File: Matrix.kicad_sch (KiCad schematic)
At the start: 28 parts

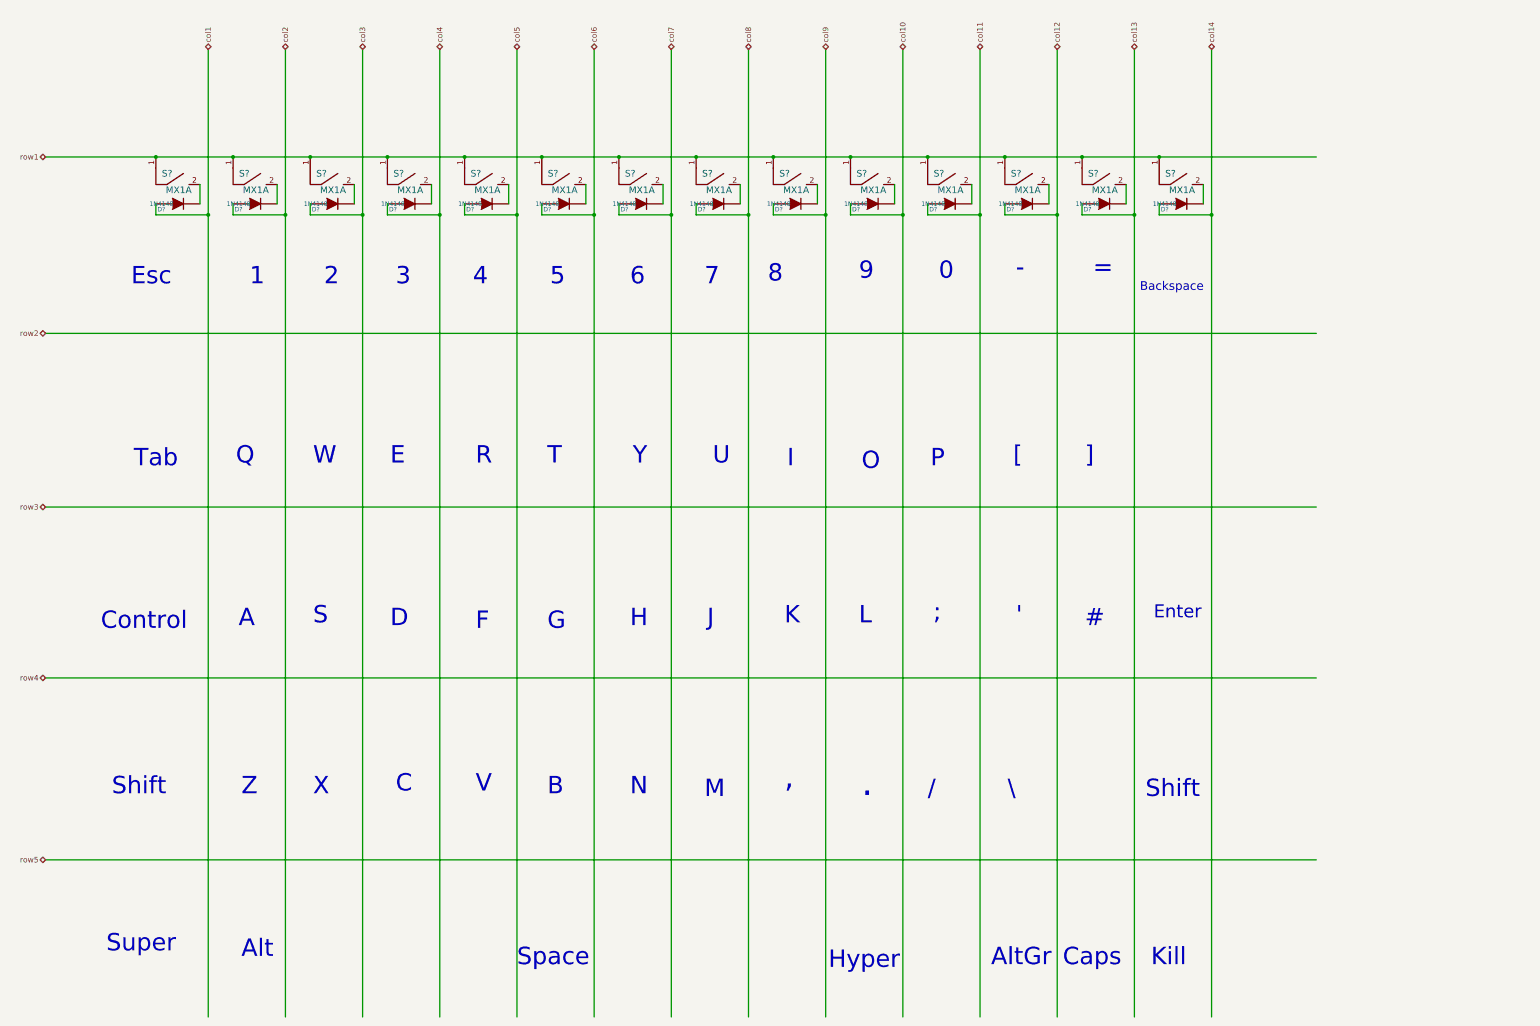
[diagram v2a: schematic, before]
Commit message: Added all remaining switches and annotations to the matrix
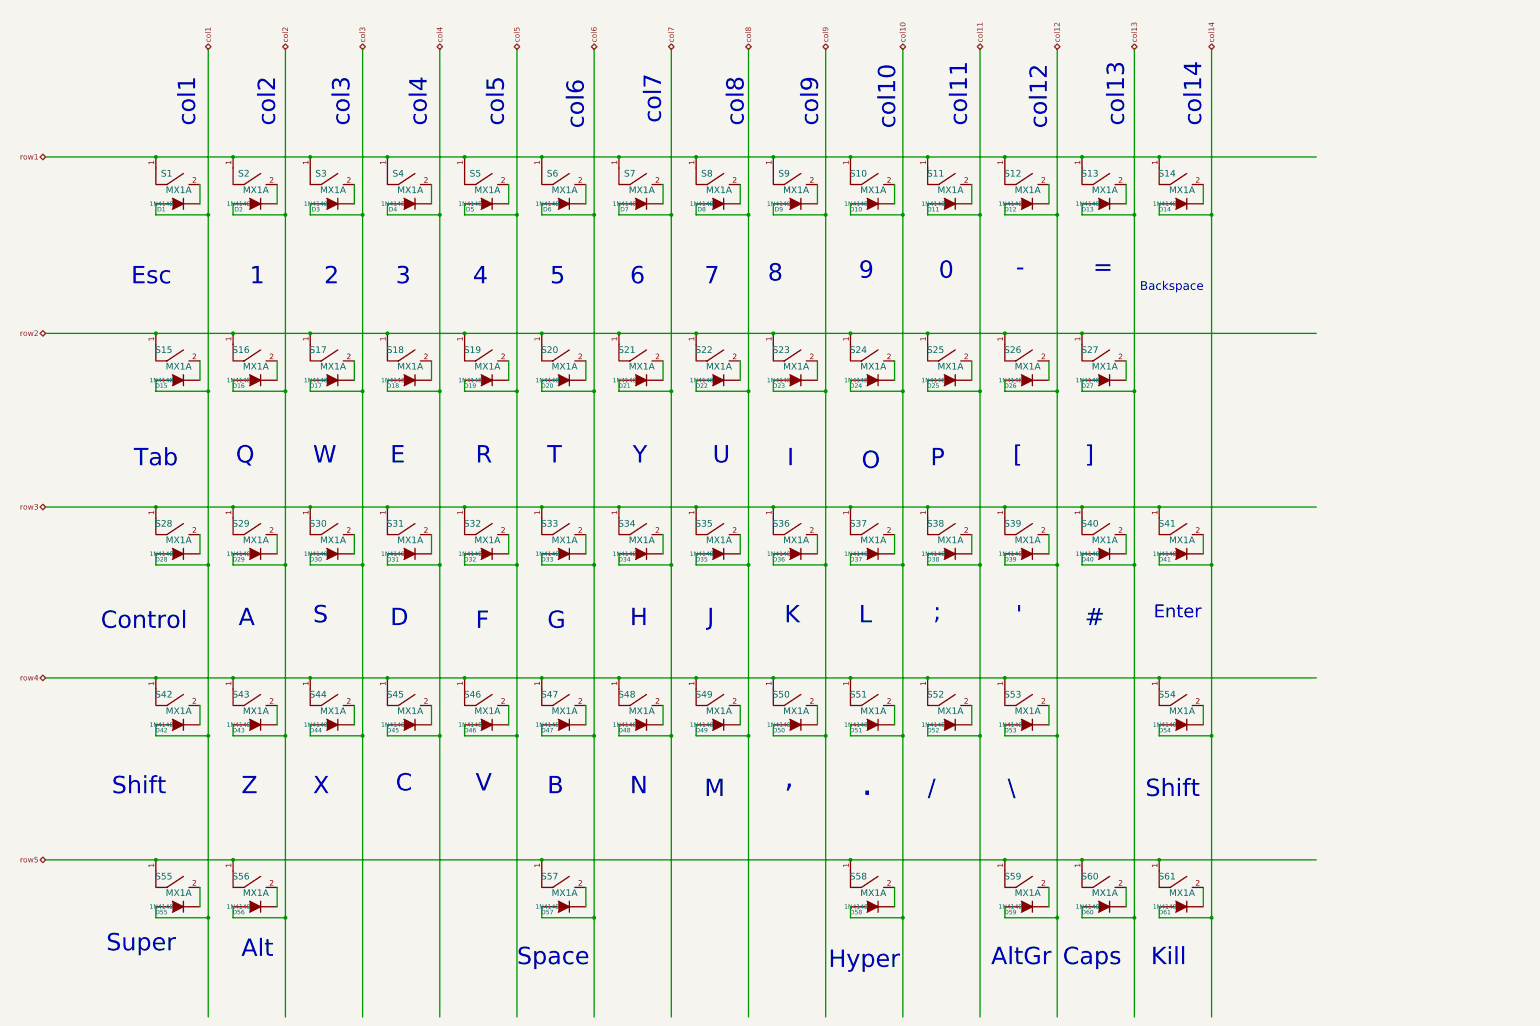
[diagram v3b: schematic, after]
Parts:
- added D15, D16, D17, D18, D19, D20, D21, D22, D23, D24, D25, D26, D27, D28, D29, D30, D31, D32, D33, D34, D35, D36, D37, D38, D39, D40, D41, D42, D43, D44, D45, D46, D47, D48, D49, D50, D51, D52, D53, D54, D55, D56, D57, D58, D59, D60, D61: 1N4148, symbol device:DIODE
- added S15, S16, S17, S18, S19, S20, S21, S22, S23, S24, S25, S26, S27, S28, S29, S30, S31, S32, S33, S34, S35, S36, S37, S38, S39, S40, S41, S42, S43, S44, S45, S46, S47, S48, S49, S50, S51, S52, S53, S54, S55, S56, S57, S58, S59, S60, S61: MX1A, symbol mx1a-simple:MX1A
- gave numbers to parts that had none: 28
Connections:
- net col1: now also D15.1 (A), D28.1 (A), D42.1 (A), D55.1 (A)
- net col10: now also D24.1 (A), D37.1 (A), D51.1 (A), D58.1 (A)
- net col11: now also D25.1 (A), D38.1 (A), D52.1 (A)
- net col12: now also D26.1 (A), D39.1 (A), D53.1 (A), D59.1 (A)
- net col13: now also D27.1 (A), D40.1 (A), D60.1 (A)
- net col14: now also D41.1 (A), D54.1 (A), D61.1 (A)
- net col2: now also D16.1 (A), D29.1 (A), D43.1 (A), D56.1 (A)
- net col3: now also D17.1 (A), D30.1 (A), D44.1 (A)
- net col4: now also D18.1 (A), D31.1 (A), D45.1 (A)
- net col5: now also D19.1 (A), D32.1 (A), D46.1 (A)
- net col6: now also D20.1 (A), D33.1 (A), D47.1 (A), D57.1 (A)
- net col7: now also D21.1 (A), D34.1 (A), D48.1 (A)
- net col8: now also D22.1 (A), D35.1 (A), D49.1 (A)
- net col9: now also D23.1 (A), D36.1 (A), D50.1 (A)
- net row2: now also S15.1, S16.1, S17.1, S18.1, S19.1, S20.1, S21.1, S22.1, S23.1, S24.1, S25.1, S26.1, S27.1
- net row3: now also S28.1, S29.1, S30.1, S31.1, S32.1, S33.1, S34.1, S35.1, S36.1, S37.1, S38.1, S39.1, S40.1, S41.1
- net row4: now also S42.1, S43.1, S44.1, S45.1, S46.1, S47.1, S48.1, S49.1, S50.1, S51.1, S52.1, S53.1, S54.1
- net row5: now also S55.1, S56.1, S57.1, S58.1, S59.1, S60.1, S61.1
- new net: D55.2 (K), S55.2
- new net: D48.2 (K), S48.2
- new net: D44.2 (K), S44.2
- new net: D32.2 (K), S32.2
- new net: D25.2 (K), S25.2
- new net: D29.2 (K), S29.2
- new net: D23.2 (K), S23.2
- new net: D21.2 (K), S21.2
- new net: D46.2 (K), S46.2
- new net: D37.2 (K), S37.2
- new net: D38.2 (K), S38.2
- new net: D19.2 (K), S19.2
- new net: D26.2 (K), S26.2
- new net: D43.2 (K), S43.2
- new net: D52.2 (K), S52.2
- new net: D31.2 (K), S31.2
- new net: D54.2 (K), S54.2
- new net: D45.2 (K), S45.2
- new net: D30.2 (K), S30.2
- new net: D28.2 (K), S28.2
- new net: D42.2 (K), S42.2
- new net: D51.2 (K), S51.2
- new net: D17.2 (K), S17.2
- new net: D24.2 (K), S24.2
- new net: D41.2 (K), S41.2
- new net: D33.2 (K), S33.2
- new net: D56.2 (K), S56.2
- new net: D15.2 (K), S15.2
- new net: D50.2 (K), S50.2
- new net: D40.2 (K), S40.2
- new net: D61.2 (K), S61.2
- new net: D53.2 (K), S53.2
- new net: D58.2 (K), S58.2
- new net: D59.2 (K), S59.2
- new net: D49.2 (K), S49.2
- new net: D22.2 (K), S22.2
- new net: D39.2 (K), S39.2
- new net: D35.2 (K), S35.2
- new net: D36.2 (K), S36.2
- new net: D60.2 (K), S60.2
- new net: D16.2 (K), S16.2
- new net: D57.2 (K), S57.2
- new net: D20.2 (K), S20.2
- new net: D34.2 (K), S34.2
- new net: D27.2 (K), S27.2
- new net: D47.2 (K), S47.2
- new net: D18.2 (K), S18.2
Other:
- note added: "col1"
- note added: "col10"
- note added: "col11"
- note added: "col12"
- note added: "col13"
- note added: "col14"
- note added: "col2"
- note added: "col3"
- note added: "col4"
- note added: "col5"
- note added: "col6"
- note added: "col7"
- note added: "col8"
- note added: "col9"

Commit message: Connected some columns to MCU and cleaned up main schema
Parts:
- S1: value MX1A -> Esc
- S10: value MX1A -> 9
- S11: value MX1A -> 0
- S12: value MX1A -> -
- S13: value MX1A -> =
- S14: value MX1A -> Backspace
- S15: value MX1A -> Tab
- S16: value MX1A -> Q
- S17: value MX1A -> W
- S18: value MX1A -> E
- S19: value MX1A -> R
- S2: value MX1A -> 1
- S20: value MX1A -> T
- S21: value MX1A -> Y
- S22: value MX1A -> U
- S23: value MX1A -> I
- S24: value MX1A -> O
- S25: value MX1A -> P
- S26: value MX1A -> [
- S27: value MX1A -> ]
- S28: value MX1A -> Control
- S29: value MX1A -> A
- S3: value MX1A -> 2
- S30: value MX1A -> S
- S31: value MX1A -> D
- S32: value MX1A -> F
- S33: value MX1A -> G
- S34: value MX1A -> H
- S35: value MX1A -> J
- S36: value MX1A -> K
- S37: value MX1A -> L
- S38: value MX1A -> ;
- S39: value MX1A -> '
- S4: value MX1A -> 3
- S40: value MX1A -> #
- S41: value MX1A -> Enter
- S42: value MX1A -> LShift
- S43: value MX1A -> Z
- S44: value MX1A -> X
- S45: value MX1A -> C
- S46: value MX1A -> V
- S47: value MX1A -> B
- S48: value MX1A -> N
- S49: value MX1A -> M
- S5: value MX1A -> 4
- S50: value MX1A -> ,
- S51: value MX1A -> .
- S52: value MX1A -> /
- S53: value MX1A -> \
- S54: value MX1A -> RShift
- S55: value MX1A -> Super
- S56: value MX1A -> Alt
- S57: value MX1A -> Space
- S58: value MX1A -> Hyper
- S59: value MX1A -> AltGraph
- S6: value MX1A -> 5
- S60: value MX1A -> Caps
- S61: value MX1A -> Kill
- S7: value MX1A -> 6
- S8: value MX1A -> 7
- S9: value MX1A -> 8

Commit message: Assigned footprints and connected all rows and columns to MCU
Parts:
- D1, D10, D11, D12, D13, D14, D15, D16, D17, D18, D19, D2, D20, D21, D22, D23, D24, D25, D26, D27, D28, D29, D3, D30, D31, D32, D33, D34, D35, D36, D37, D38, D39, D4, D40, D41, D42, D43, D44, D45, D46, D47, D48, D49, D5, D50, D51, D52, D53, D54, D55, D56, D57, D58, D59, D6, D60, D61, D7, D8, D9: footprint (none) -> Diode_SMD:D_SOD-123
- S1, S10, S11, S12, S13, S16, S17, S18, S19, S2, S20, S21, S22, S23, S24, S25, S26, S27, S29, S3, S30, S31, S32, S33, S34, S35, S36, S37, S38, S39, S4, S40, S43, S44, S45, S46, S47, S48, S49, S5, S50, S51, S52, S53, S6, S60, S61, S7, S8, S9: footprint (none) -> MX_Alps_Hybrid:MX-1U
- S14, S42, S54: footprint (none) -> MX_Alps_Hybrid:MX-2U
- S15: footprint (none) -> MX_Alps_Hybrid:MX-1.5U
- S28, S55, S56, S58: footprint (none) -> MX_Alps_Hybrid:MX-1.75U
- S41: footprint (none) -> MX_Alps_Hybrid:MX-ISO
- S57: footprint (none) -> MX_Alps_Hybrid:MX-6.5U
- S59: footprint (none) -> MX_Alps_Hybrid:MX-1.25U
